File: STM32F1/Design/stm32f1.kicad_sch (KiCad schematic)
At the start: 17 parts, among them P1 USB_C_Plug_USB2.0, SW1 SW_SPDT, U1 STM32F103C8Tx, Y1 16MHz

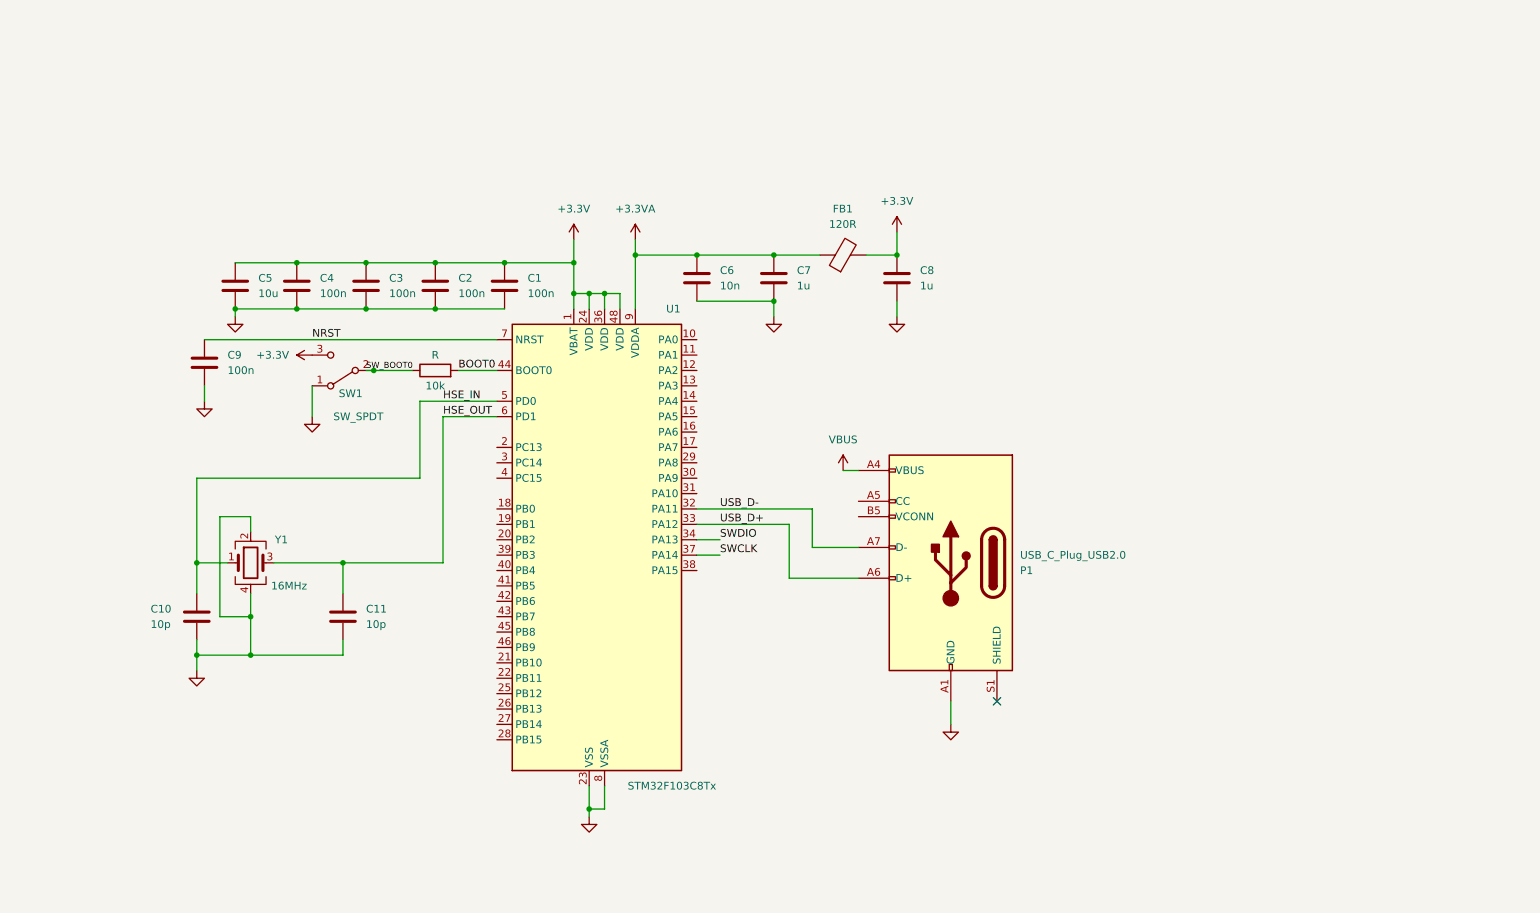
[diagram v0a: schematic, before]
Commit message: Added power and pinout circuit
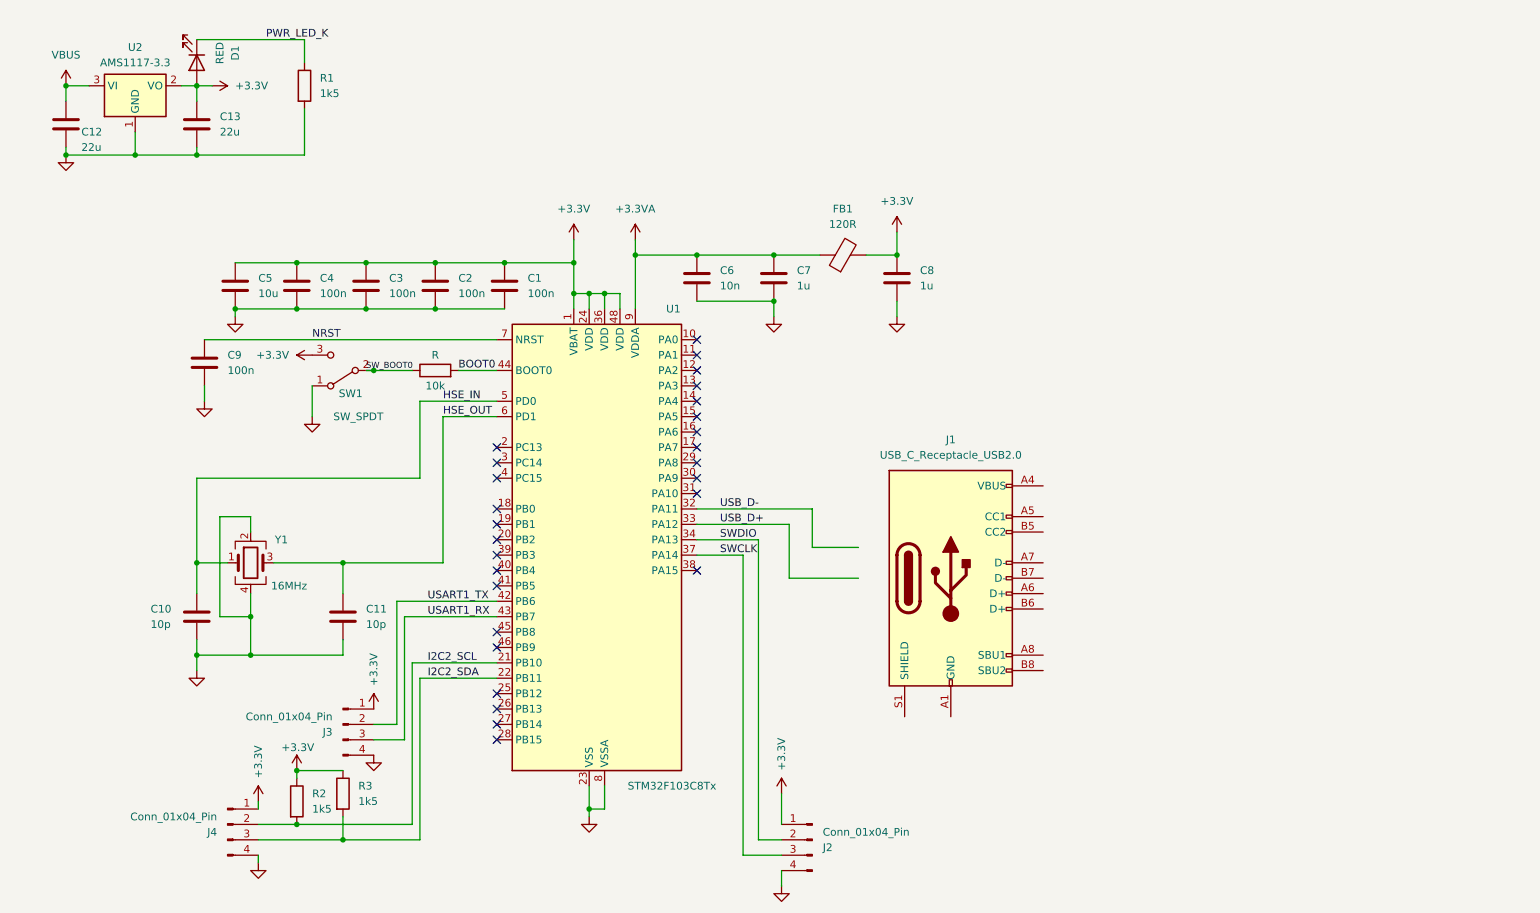
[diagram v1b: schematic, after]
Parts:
- removed P1: USB_C_Plug_USB2.0, symbol Connector:USB_C_Plug_USB2.0
- added C12, C13: 22u, symbol Device:C
- added D1: RED, symbol Device:LED
- added J1: USB_C_Receptacle_USB2.0, symbol Connector:USB_C_Receptacle_USB2.0
- added J2, J3, J4: Conn_01x04_Pin, symbol Connector:Conn_01x04_Pin
- added R1, R2, R3: 1k5, symbol Device:R
- added U2: AMS1117-3.3, Package_TO_SOT_SMD:SOT-223-3_TabPin2, symbol Regulator_Linear:AMS1117-3.3
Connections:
- net +3.3V: now also C13.1, D1.2 (A), J2.1 (Pin_1), J3.1 (Pin_1), J4.1 (Pin_1), R2.1, R3.1, U2.2 (VO)
- net GND: now also C12.2, C13.2, J2.4 (Pin_4), J3.4 (Pin_4), J4.4 (Pin_4), R1.2, U2.1 (GND)
- net SWCLK: now also J2.3 (Pin_3)
- net SWDIO: now also J2.2 (Pin_2)
- net VBUS: now also C12.1, U2.3 (VI)
- net I2C2_SCL: now reaches U1.21 (PB10)
- net I2C2_SCL: now also J4.2 (Pin_2), R2.2
- net I2C2_SDA: now reaches U1.22 (PB11)
- net I2C2_SDA: now also J4.3 (Pin_3), R3.2
- net USART1_TX: now reaches U1.42 (PB6)
- net USART1_TX: now also J3.2 (Pin_2)
- net USART1_RX: now reaches U1.43 (PB7)
- net USART1_RX: now also J3.3 (Pin_3)
- new net: J1.A1 (GND), J1.A12 (GND), J1.B1 (GND), J1.B12 (GND)
- new net: J1.A4 (VBUS), J1.A9 (VBUS), J1.B4 (VBUS), J1.B9 (VBUS)
- new net PWR_LED_K: D1.1 (K), R1.1
- no-connect marks 1 -> 27

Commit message: Completed schematics and added PCB layout
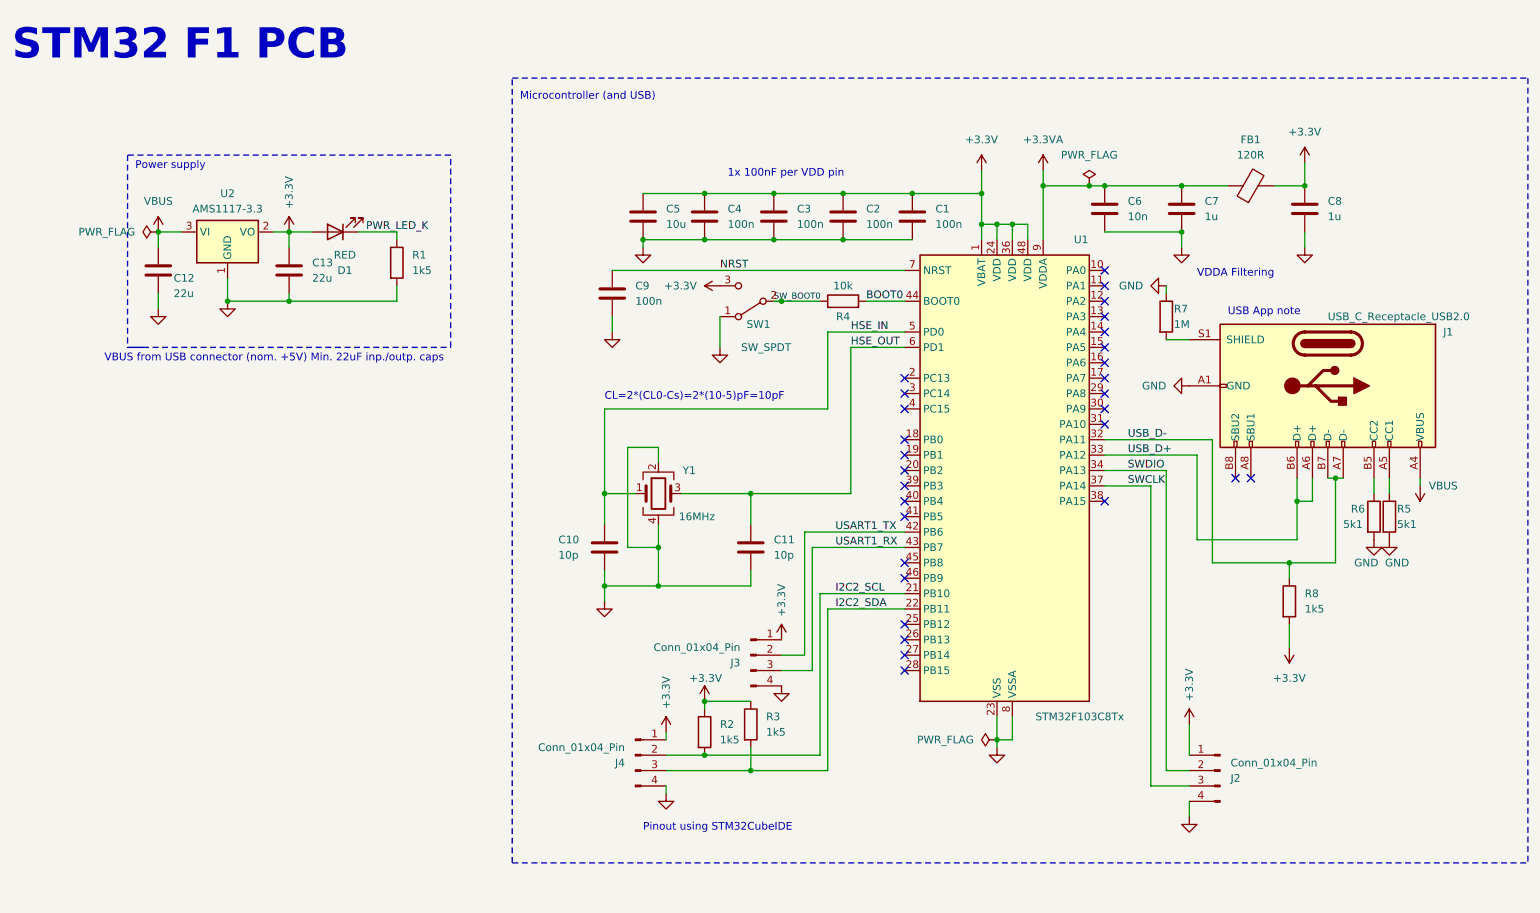
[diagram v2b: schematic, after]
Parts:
- added R5, R6: 5k1, Resistor_SMD:R_0402_1005Metric, symbol Device:R
- added R7: 1M, Resistor_SMD:R_0402_1005Metric, symbol Device:R
- added R8: 1k5, Resistor_SMD:R_0402_1005Metric, symbol Device:R
- C1, C10, C11, C2, C3, C4, C6, C7, C8, C9: footprint (none) -> Capacitor_SMD:C_0402_1005Metric
- C12, C13: footprint (none) -> Capacitor_SMD:C_0805_2012Metric
- C5: footprint (none) -> Capacitor_SMD:C_0603_1608Metric
- D1: footprint (none) -> LED_SMD:LED_0603_1608Metric
- FB1: footprint (none) -> Inductor_SMD:L_0603_1608Metric
- J1: footprint (none) -> Connector_USB:USB_C_Receptacle_Molex_105450-0101
- J2, J3, J4: footprint (none) -> Connector_PinHeader_2.54mm:PinHeader_1x04_P2.54mm_Vertical
- R1, R2, R3: footprint (none) -> Resistor_SMD:R_0402_1005Metric
- R4: renamed from 10k; value R -> 10k; footprint (none) -> Resistor_SMD:R_0402_1005Metric
- SW1: footprint (none) -> Button_Switch_SMD:SW_SPDT_PCM12
- Y1: footprint (none) -> Crystal:Crystal_SMD_3225-4Pin_3.2x2.5mm
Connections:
- net +3.3V: now also R8.2
- net GND: now also J1.A1 (GND), J1.A12 (GND), J1.B1 (GND), J1.B12 (GND), R5.2, R6.2, R7.1
- net USB_D+: now also J1.A6 (D+), J1.B6 (D+)
- net USB_D-: now also J1.A7 (D-), J1.B7 (D-), R8.1
- net VBUS: now also J1.A4 (VBUS), J1.A9 (VBUS), J1.B4 (VBUS), J1.B9 (VBUS)
- net at J1.A5 (CC1): now also R5.1
- net at J1.B5 (CC2): now also R6.1
- net at J1.S1 (SHIELD): now also R7.2
- no-connect marks 27 -> 29
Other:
- note added: "1x 100nF per VDD pin"
- note added: "CL=2*(CL0-Cs)=2*(10-5)pF=10pF"
- note added: "Microcontroller (and USB)"
- note added: "Pinout using STM32CubeIDE"
- note added: "Power supply"
- note added: "STM32 F1 PCB"
- note added: "USB App note"
- note added: "VBUS from USB connector (nom. +5V) Min. 22uF inp./outp. caps"
- note added: "VDDA Filtering"
- title: (none) -> STM32 F1 PCB
- moved on the sheet: C1, C10, C11, C12, C13, C2, C3, C4, C5, C6, C7, C8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

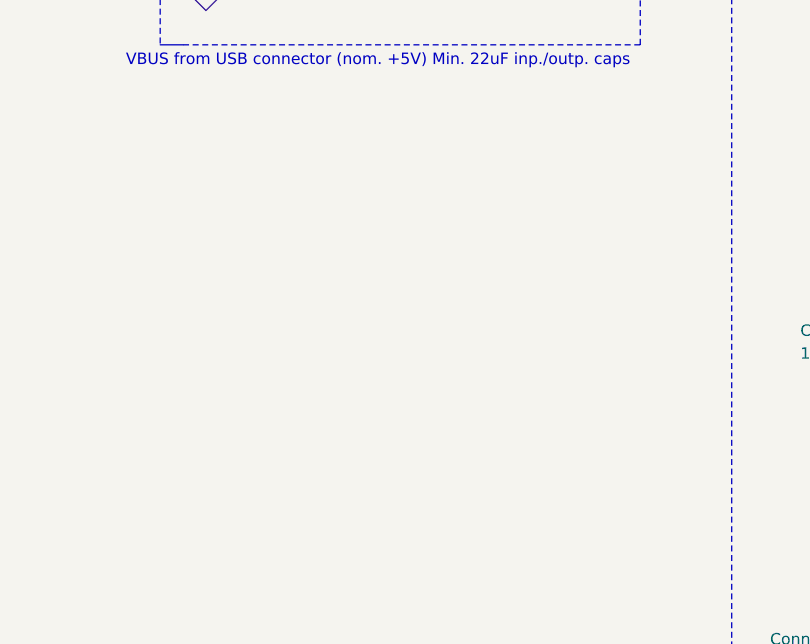
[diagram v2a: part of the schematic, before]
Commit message: Fine tunes PCB layout and added borders, Started routing
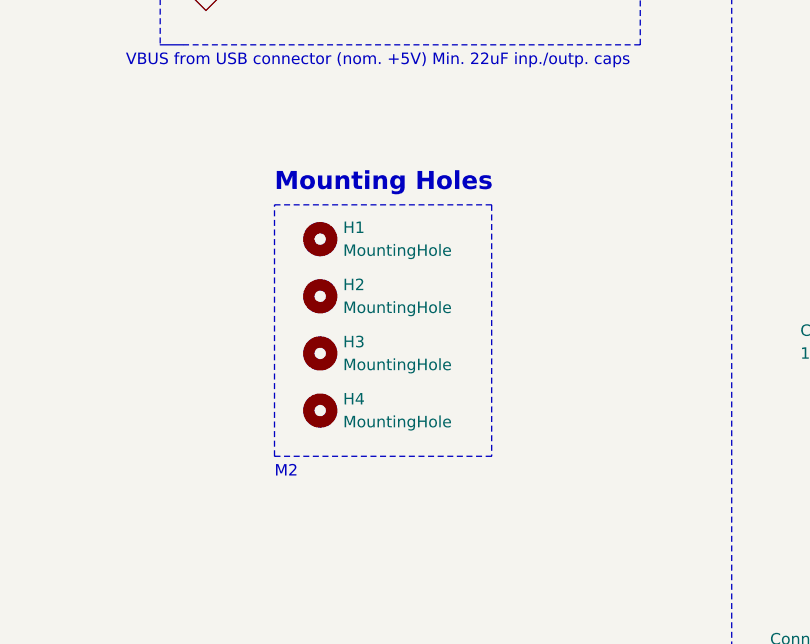
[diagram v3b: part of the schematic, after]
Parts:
- added H1, H2, H3, H4: MountingHole, MountingHole:MountingHole_2.2mm_M2, symbol Mechanical:MountingHole
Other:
- note added: "M2"
- note added: "Mounting Holes"
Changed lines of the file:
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@@
     (stroke (width 0) (type default))
   )
+  (rectangle (start 45.72 87.63) (end 69.85 115.57)
+    (stroke (width 0) (type dash))
+    (fill (type none))
+  )
   (text "Power supply" (at 34.29 40.64 0)
+    (effects (font (size 1.27 1.27)) (justify left bottom))
+  )
+  (text "M2" (at 45.72 118.11 0)
     (effects (font (size 1.27 1.27)) (justify left bottom))
   )
@@
     (effects (font (size 5 5) (thickness 1.4) bold) (justify left bottom))
   )
+  (text "Mounting Holes" (at 45.72 86.36 0)
+    (effects (font (size 2 2) (thickness 0.4) bold) (justify left bottom))
+  )
   (label "USART1_RX" (at 149.86 102.87 0) (fields_autoplaced)
     (effects (font (size 1.27 1.27)) (justify left bottom))
@@
         (path "/a5bd2ae5-739a-4024-8a9a-bd87d8d2ba41"
           (reference "C13") (unit 1)
+        )
+      )
+    )
+  )
+  (symbol (lib_id "Mechanical:MountingHole") (at 50.8 110.49 0) (unit 1)
+    (in_bom yes) (on_board yes) (dnp no) (fields_autoplaced)
+    (property "Reference" "H4" (at 53.34 109.22 0)
+      (effects (font (size 1.27 1.27)) (justify left))
+    )
+    (property "Value" "MountingHole" (at 53.34 111.76 0)
+      (effects (font (size 1.27 1.27)) (justify left))
+    )
+    (property "Footprint" "MountingHole:MountingHole_2.2mm_M2" (at 50.8 110.49 0)
+      (effects (font (size 1.27 1.27)) hide)
+    )
+    (property "Datasheet" "~" (at 50.8 110.49 0)
+      (effects (font (size 1.27 1.27)) hide)
+    )
+    (instances
+      (project "stm32f1"
+        (path "/a5bd2ae5-739a-4024-8a9a-bd87d8d2ba41"
+          (reference "H4") (unit 1)
         )
       )
@@
     )
   )
+  (symbol (lib_id "Mechanical:MountingHole") (at 50.8 91.44 0) (unit 1)
+    (in_bom yes) (on_board yes) (dnp no) (fields_autoplaced)
+    (property "Reference" "H1" (at 53.34 90.17 0)
+      (effects (font (size 1.27 1.27)) (justify left))
+    )
+    (property "Value" "MountingHole" (at 53.34 92.71 0)
+      (effects (font (size 1.27 1.27)) (justify left))
+    )
+    (property "Footprint" "MountingHole:MountingHole_2.2mm_M2" (at 50.8 91.44 0)
+      (effects (font (size 1.27 1.27)) hide)
+    )
+    (property "Datasheet" "~" (at 50.8 91.44 0)
+      (effects (font (size 1.27 1.27)) hide)
+    )
+    (instances
+      (project "stm32f1"
+        (path "/a5bd2ae5-739a-4024-8a9a-bd87d8d2ba41"
+          (reference "H1") (unit 1)
+        )
+      )
+    )
+  )
   (symbol (lib_id "Device:C") (at 139.7 48.26 0) (unit 1)
     (in_bom yes) (on_board yes) (dnp no) (fields_autoplaced)
@@
         (path "/a5bd2ae5-739a-4024-8a9a-bd87d8d2ba41"
           (reference "R3") (unit 1)
+        )
+      )
+    )
+  )
+  (symbol (lib_id "Mechanical:MountingHole") (at 50.8 97.79 0) (unit 1)
+    (in_bom yes) (on_board yes) (dnp no) (fields_autoplaced)
+    (property "Reference" "H2" (at 53.34 96.52 0)
+      (effects (font (size 1.27 1.27)) (justify left))
+    )
+    (property "Value" "MountingHole" (at 53.34 99.06 0)
+      (effects (font (size 1.27 1.27)) (justify left))
+    )
+    (property "Footprint" "MountingHole:MountingHole_2.2mm_M2" (at 50.8 97.79 0)
+      (effects (font (size 1.27 1.27)) hide)
+    )
+    (property "Datasheet" "~" (at 50.8 97.79 0)
+      (effects (font (size 1.27 1.27)) hide)
+    )
+    (instances
+      (project "stm32f1"
+        (path "/a5bd2ae5-739a-4024-8a9a-bd87d8d2ba41"
+          (reference "H2") (unit 1)
         )
       )
@@
         )
       )
+    )
+  )
+  (symbol (lib_id "Mechanical:MountingHole") (at 50.8 104.14 0) (unit 1)
+    (in_bom yes) (on_board yes) (dnp no) (fields_autoplaced)
+    (property "Reference" "H3" (at 53.34 102.87 0)
+      (effects (font (size 1.27 1.27)) (justify left))
+    )
+    (property "Value" "MountingHole" (at 53.34 105.41 0)
+      (effects (font (size 1.27 1.27)) (justify left))
+    )
+    (property "Footprint" "MountingHole:MountingHole_2.2mm_M2" (at 50.8 104.14 0)
+      (effects (font (size 1.27 1.27)) hide)
+    )
+    (property "Datasheet" "~" (at 50.8 104.14 0)
+      (effects (font (size 1.27 1.27)) hide)
+    )
+    (instances
+      (project "stm32f1"
+        (path "/a5bd2ae5-739a-4024-8a9a-bd87d8d2ba41"
+          (reference "H3") (unit 1)
+        )
+      )

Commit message: Completed Board design
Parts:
- J1: footprint Connector_USB:USB_C_Receptacle_Molex_105450-0101 -> Connector_USB:USB_C_Receptacle_HRO_TYPE-C-31-M-12
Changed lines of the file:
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@@
       (effects (font (size 1.27 1.27)) (justify left))
     )
-    (property "Footprint" "Connector_USB:USB_C_Receptacle_Molex_105450-0101" (at 231.14 80.01 0)
+    (property "Footprint" "Connector_USB:USB_C_Receptacle_HRO_TYPE-C-31-M-12" (at 231.14 80.01 0)
       (effects (font (size 1.27 1.27)) hide)
     )
